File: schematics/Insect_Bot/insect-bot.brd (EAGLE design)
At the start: 45.4 x 81.3 mm, 28 parts, among them Q1 2N2222, U1 L4931-TO92-AMMO, U2 ARDUINO_MINI

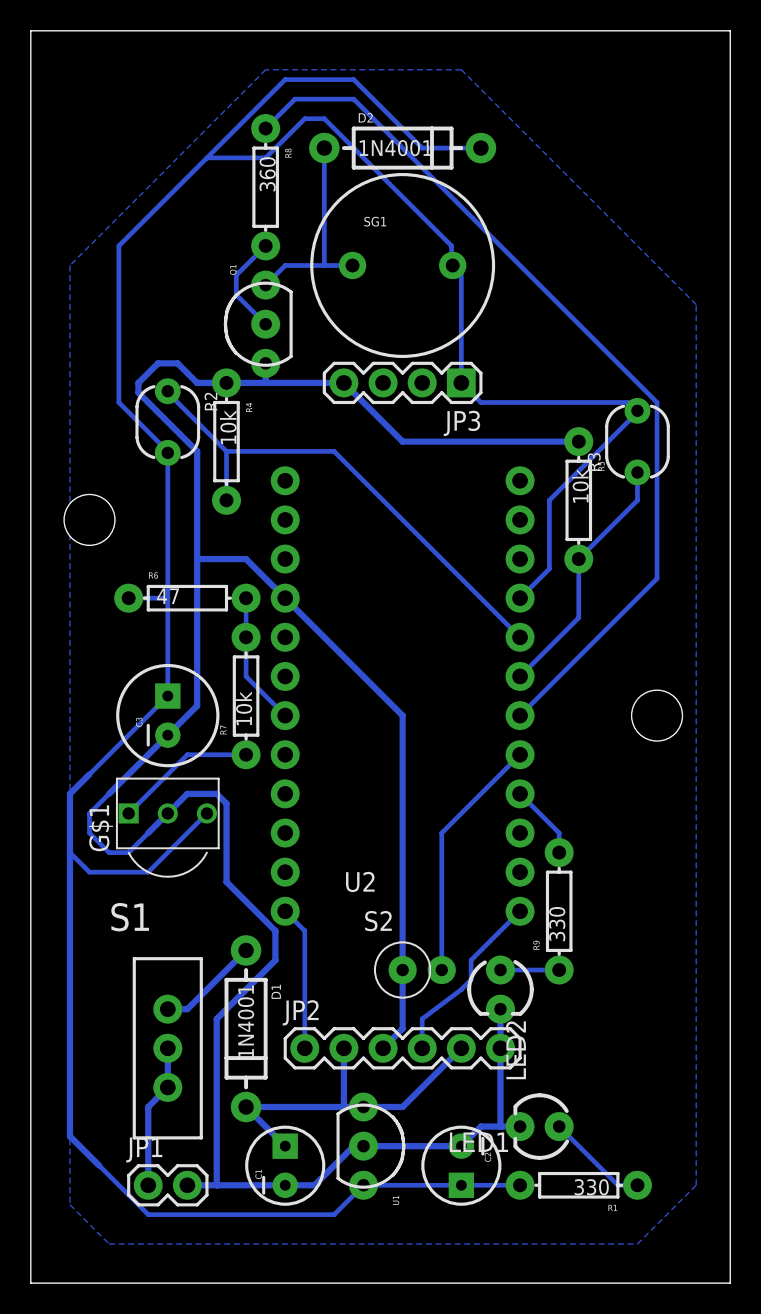
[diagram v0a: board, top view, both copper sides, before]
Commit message: Finished board layout.
Spaced out close traces. Added a ground plane.
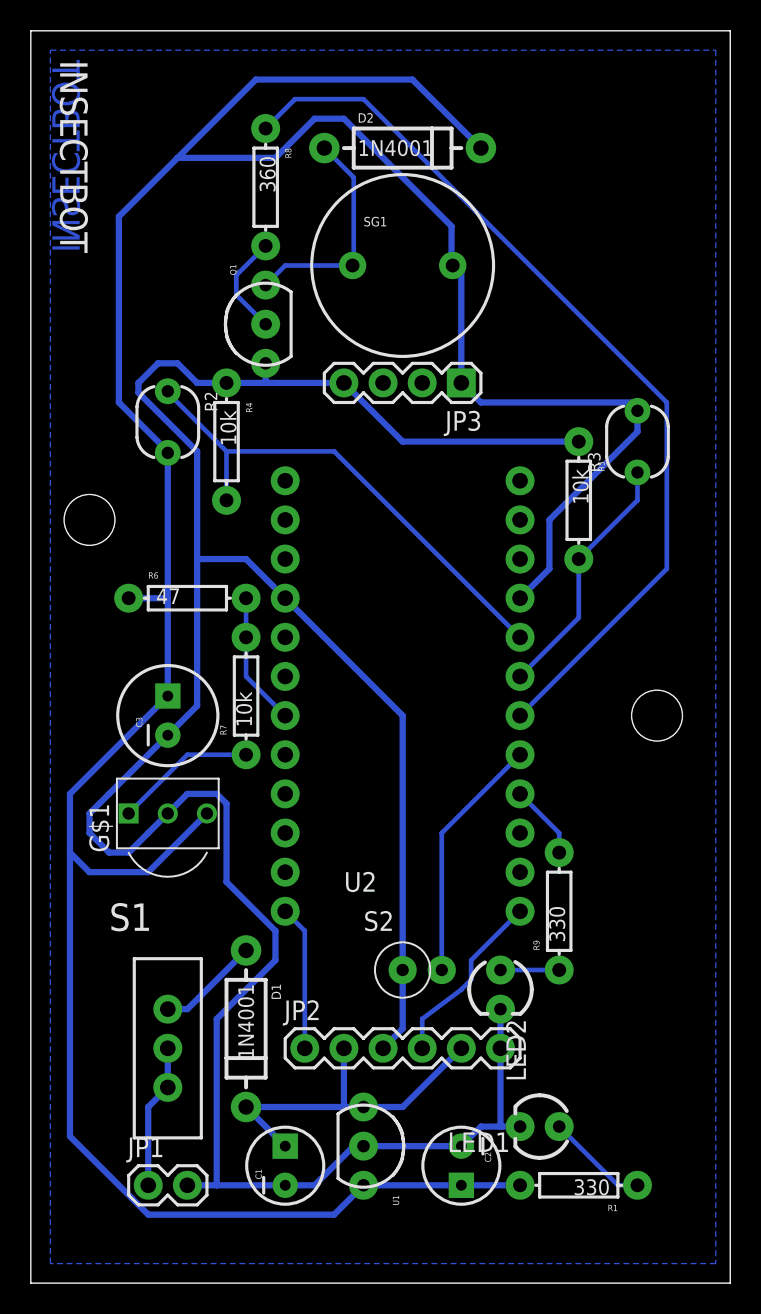
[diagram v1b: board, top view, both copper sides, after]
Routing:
- net VCC: track 194.9 -> 198.7 mm
- net N$6: track 58.3 -> 59.2 mm
- net N$11: track 13.8 -> 14.6 mm
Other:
- board text added: "INSECTBOT"

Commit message: Made traces thicker.
Upped power net traces to 32 mil with 16 mil clearance and signal
net traces to 24 mil with 16 mil clearance.
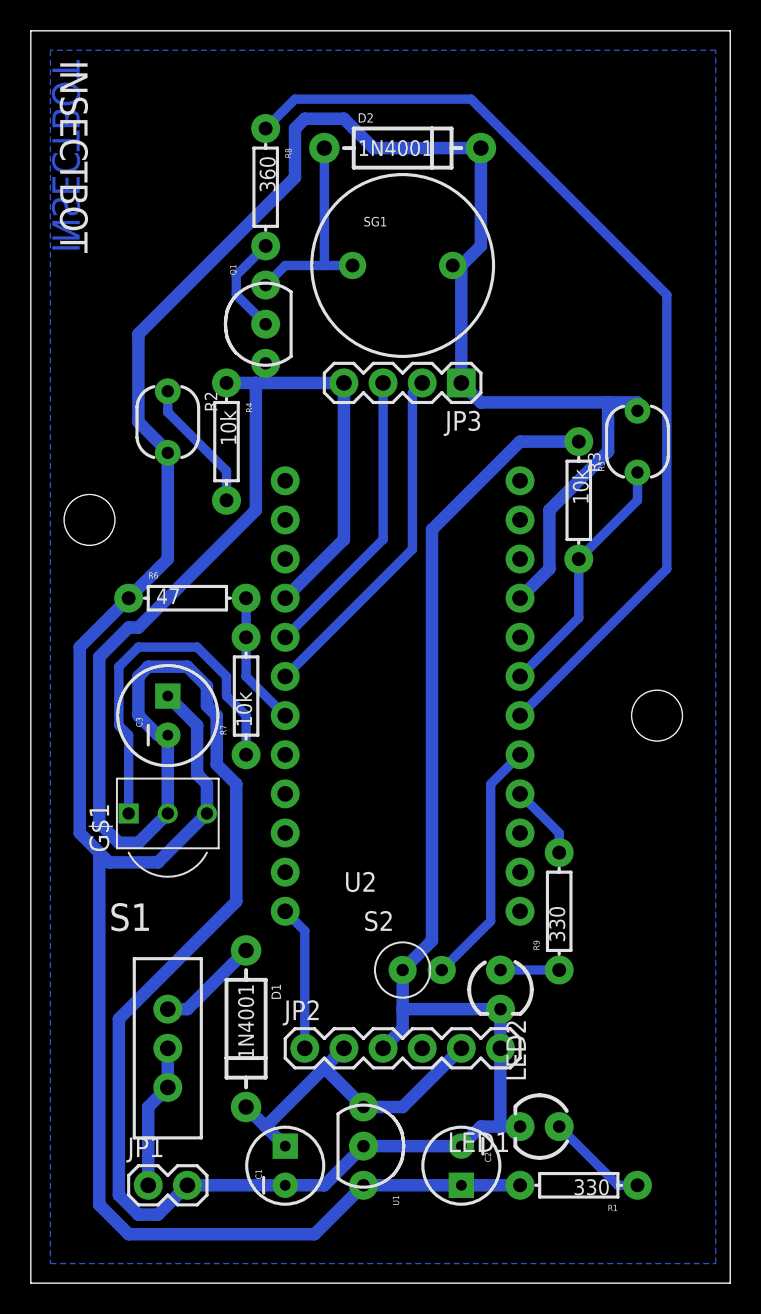
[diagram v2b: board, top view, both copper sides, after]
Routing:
- net GND: track 175.5 -> 205.4 mm
- net N$8: track 32.7 -> 8.66 mm
- net TRIGGER: track 0.00 -> 22.7 mm
- net ECHO: track 0.00 -> 19.1 mm
- net VCC: track 198.7 -> 181.4 mm
- net REMOTE: track 9.20 -> 23.7 mm
- net N$5: track 11.7 -> 0.00 mm
- net N$6: track 59.2 -> 63.3 mm
- net N$11: track 14.6 -> 13.8 mm
- net V_IN: track 23.0 -> 22.3 mm

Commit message: Final layout for insect bot board.
Made traces a bit wider. Increased size of pad for the IR remote
receiver.
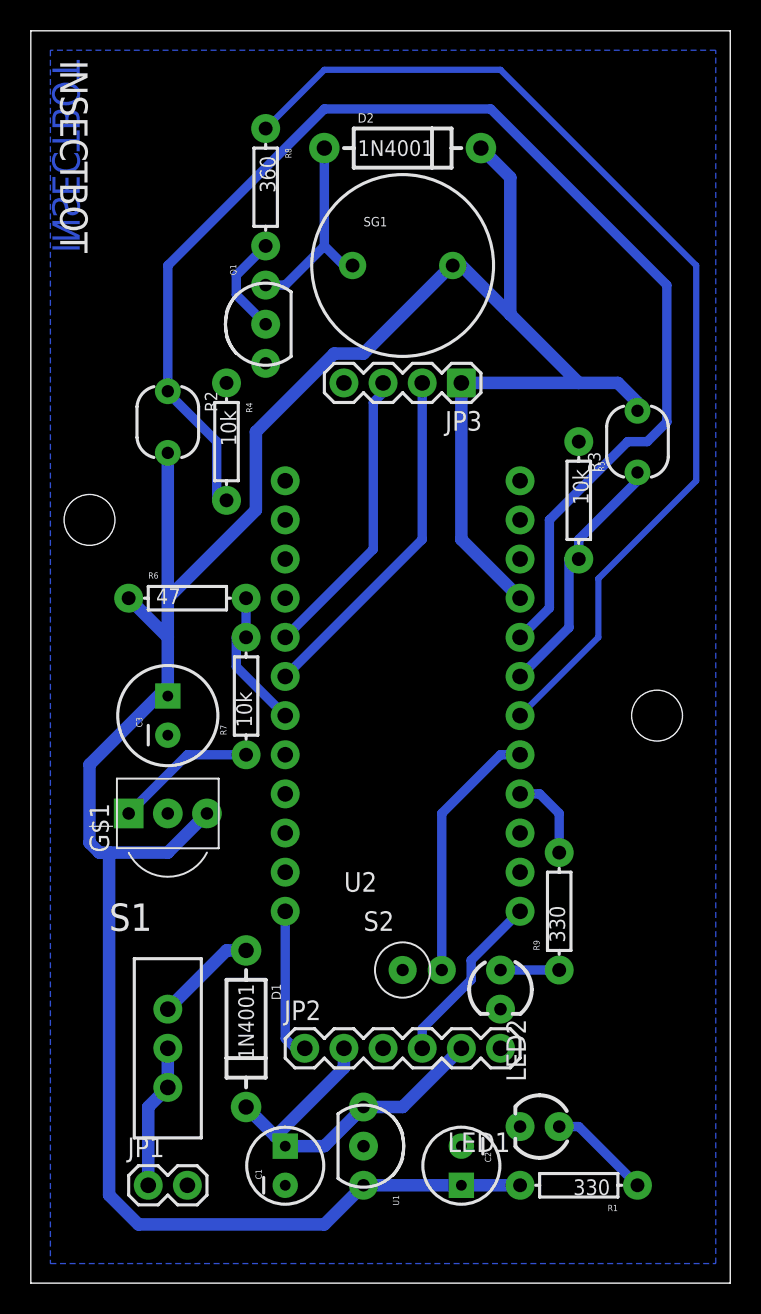
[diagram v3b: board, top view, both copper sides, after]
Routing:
- net GND: track 205.4 -> 0.00 mm
- net N$8: track 8.66 -> 86.1 mm
- net REMOTE: track 23.7 -> 9.20 mm
- net N$5: track 0.00 -> 11.5 mm
- net VCC: track 181.4 -> 172.7 mm
- net N$6: track 63.3 -> 68.7 mm
- net V_IN: track 22.3 -> 25.2 mm
- net N$9: track 8.67 -> 9.83 mm
- net N$13: track 4.86 -> 5.61 mm
- net N$12: track 16.1 -> 16.8 mm
- net N$7: track 16.4 -> 17.0 mm
